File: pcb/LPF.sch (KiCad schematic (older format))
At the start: 5 parts

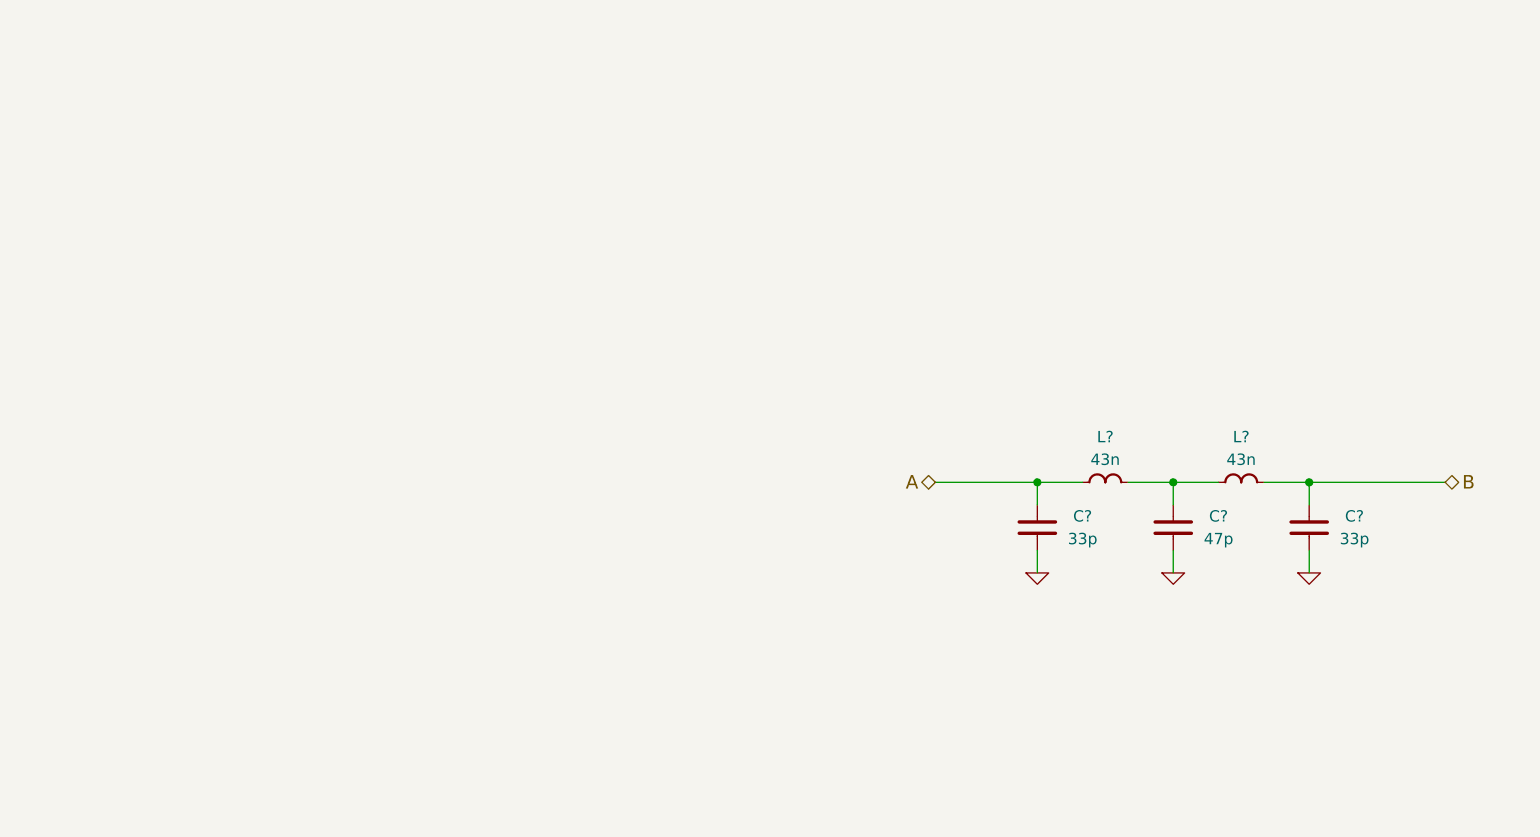
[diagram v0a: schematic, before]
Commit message: Copper is likely complete
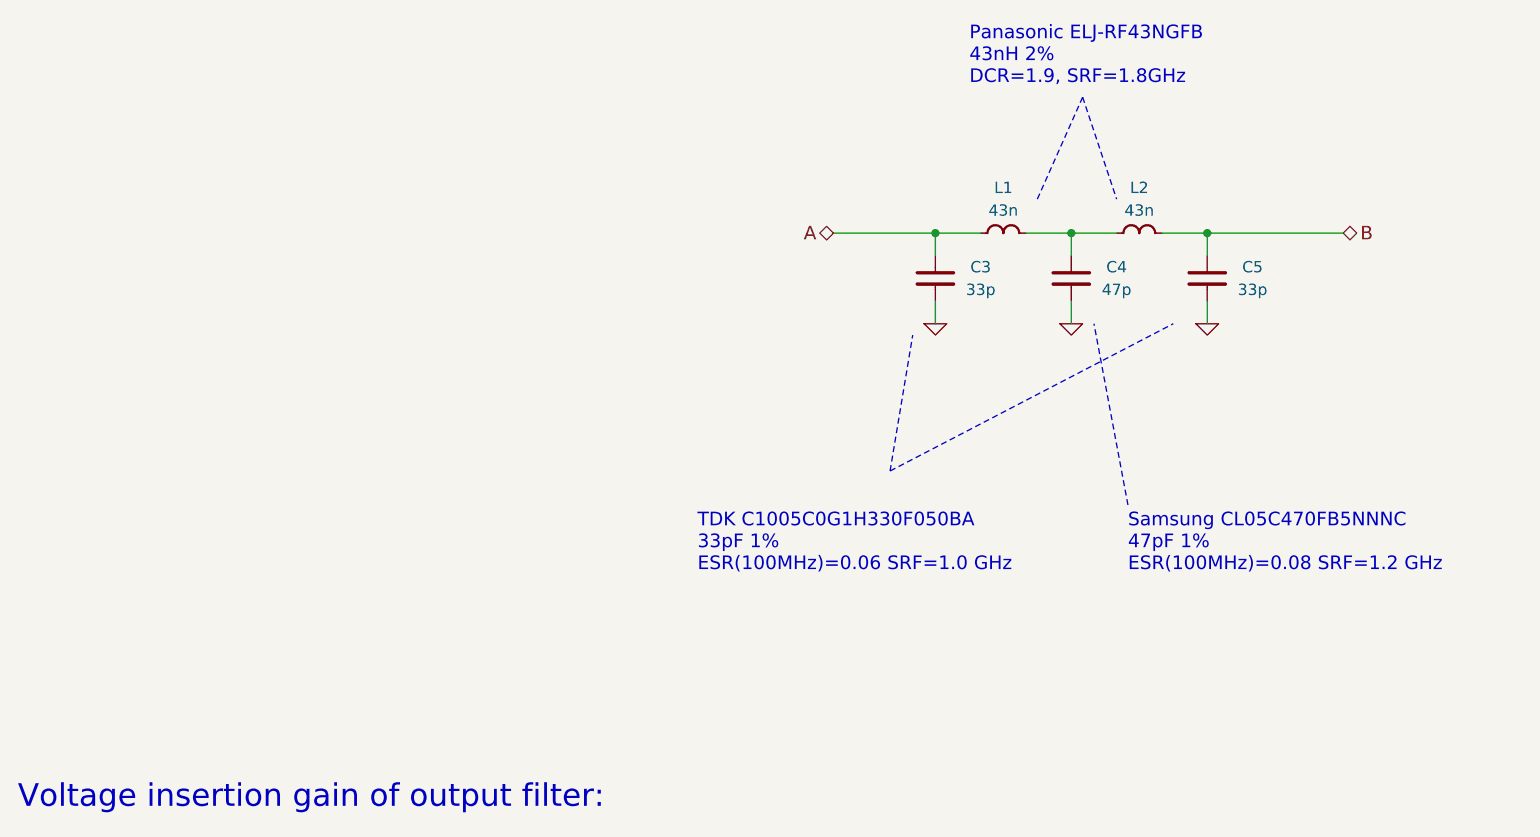
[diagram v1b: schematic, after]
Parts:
- removed L? (x2): 43n, symbol L
- added L1, L2: 43n, IPC7351-Nominal:INDC1005X60, symbol L-0402
- C3, C4, C5: renamed from C?; footprint (none) -> IPC7351-Nominal:CAPC1005X55
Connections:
- net A: now also L1.2
- net B: now also L2.1
- net at C4.1: now also L1.1, L2.2
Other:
- note added: "Panasonic ELJ-RF43NGFB\n43nH 2%\nDCR=1.9, SRF=1.8GHz"
- note added: "Samsung CL05C470FB5NNNC\n47pF 1%\nESR(100MHz)=0.08 SRF=1.2 GHz"
- note added: "TDK C1005C0G1H330F050BA\n33pF 1%\nESR(100MHz)=0.06 SRF=1.0 GHz"
- note added: "Voltage insertion gain of output filter:"
- moved on the sheet: C3, C4, C5
